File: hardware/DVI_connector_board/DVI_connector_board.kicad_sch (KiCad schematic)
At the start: 3 parts, among them J1 FPC Cable connector 1x20, J2 HDMI_A

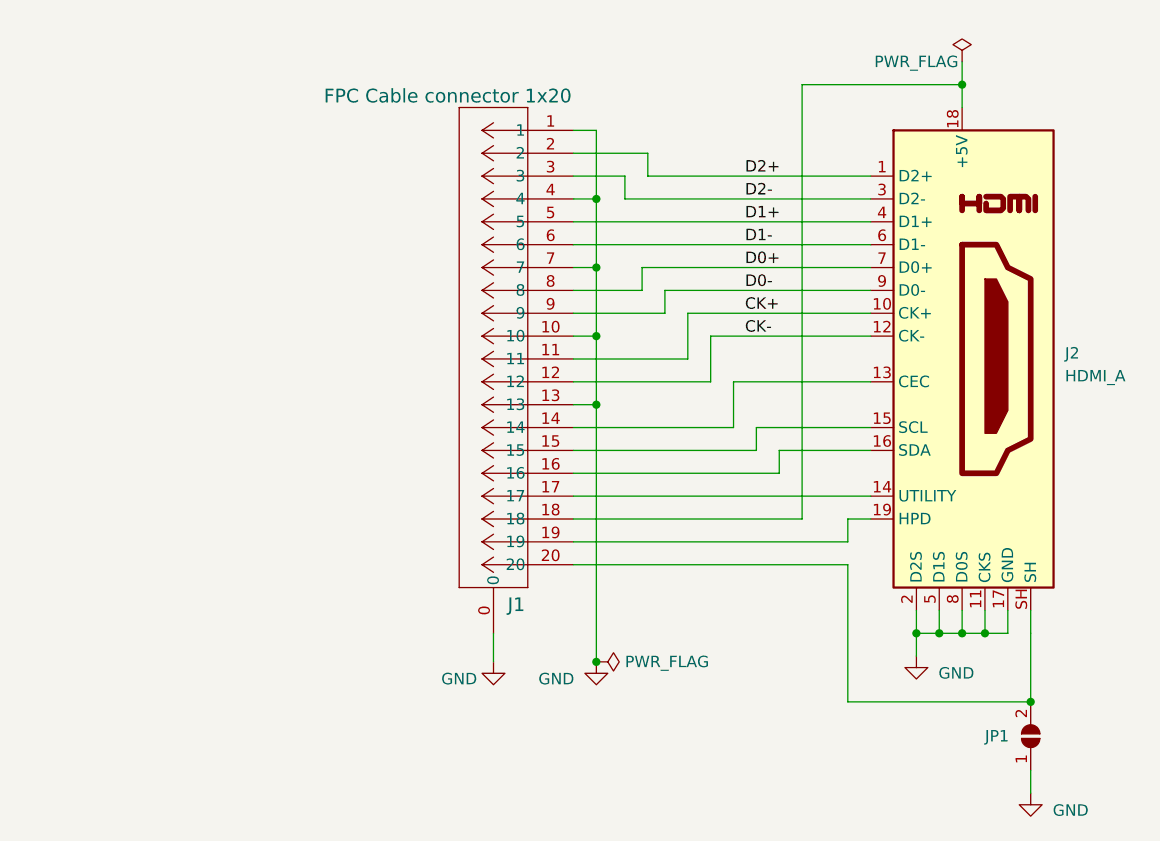
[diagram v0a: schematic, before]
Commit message: Change pinout for being compatible with common extension cables
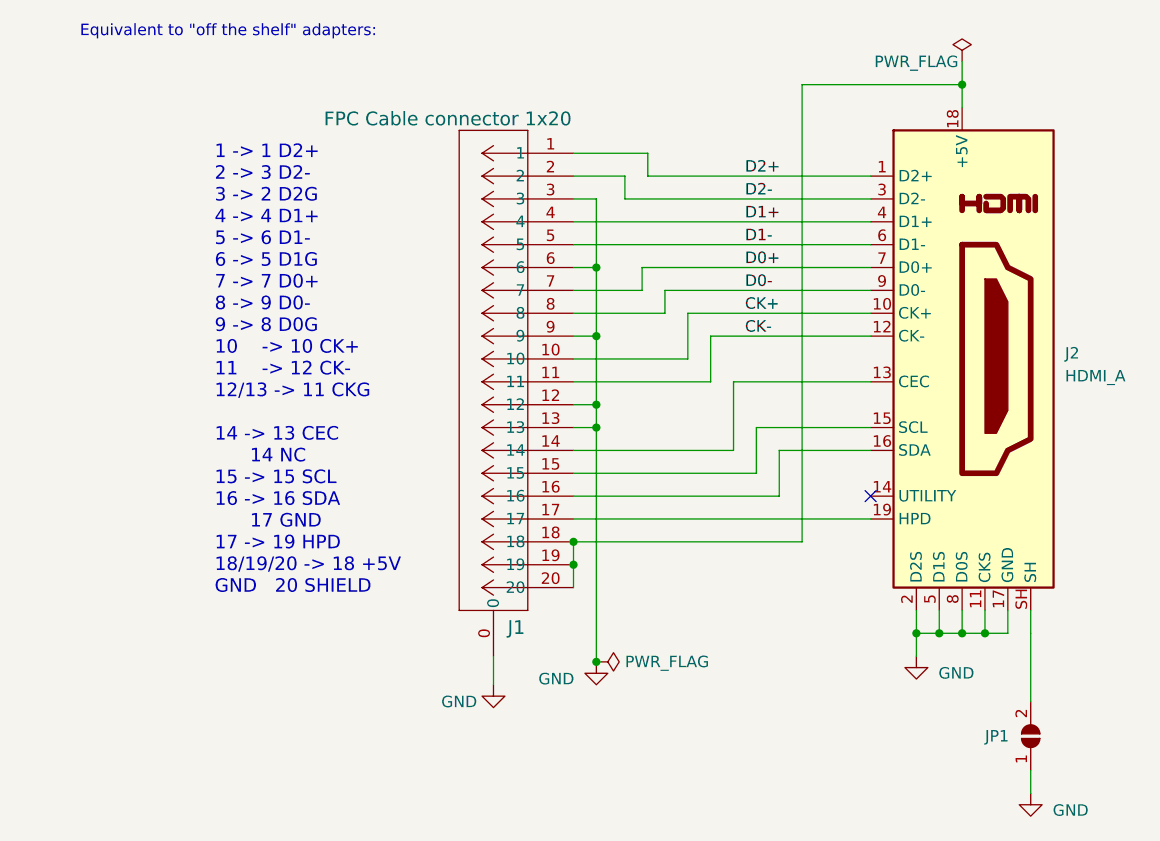
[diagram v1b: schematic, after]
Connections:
- net CK+: now also J1.10; no longer J1.11
- net CK-: now also J1.11; no longer J1.12
- net D0+: now also J1.7; no longer J1.8
- net D0-: now also J1.8; no longer J1.9
- net D1+: now also J1.4; no longer J1.5
- net D1-: now also J1.5; no longer J1.6
- net D2+: now also J1.1; no longer J1.2
- net D2-: now also J1.2; no longer J1.3
- net GND: now also J1.12, J1.3, J1.6, J1.9; no longer J1.1, J1.10, J1.4, J1.7
- net at J2.14 (UTILITY): no longer J1.17
- net at J1.18, J2.18 (+5V): now also J1.19, J1.20
- net at J2.19 (HPD): now also J1.17; no longer J1.19
- net at J2.SH, JP1.2 (B): no longer J1.20
- no-connect marks 0 -> 1
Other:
- note added: "1 -> 1 D2+ 2 -> 3 D2- 3 -> 2 D2G 4 -> 4 D1+ 5 -> 6 D1- 6 -> 5 D1G 7 -> 7 D0+ 8 -> 9 D0- 9 -> 8 D0G 10 -> 10 CK+ 11 -> 12 CK- 12/13 -> 11 CKG 14 -> 13 CEC 14 NC 15 -> 15 SCL 16 -> 16 SDA 17 GND 17 -> 19 HPD 18/19/20 -> 18 +5V GND 20 SHIELD"
- note added: "Equivalent to "off the shelf" adapters:"
